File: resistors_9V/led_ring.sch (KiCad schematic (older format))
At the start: 15 parts, among them J1 Conn_01x02

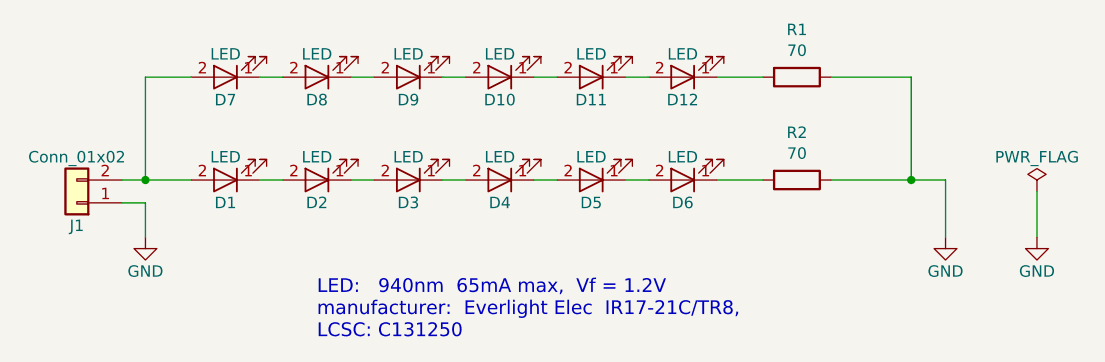
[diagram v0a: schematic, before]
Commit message: Finished 9V design w/ current limiting resistors.
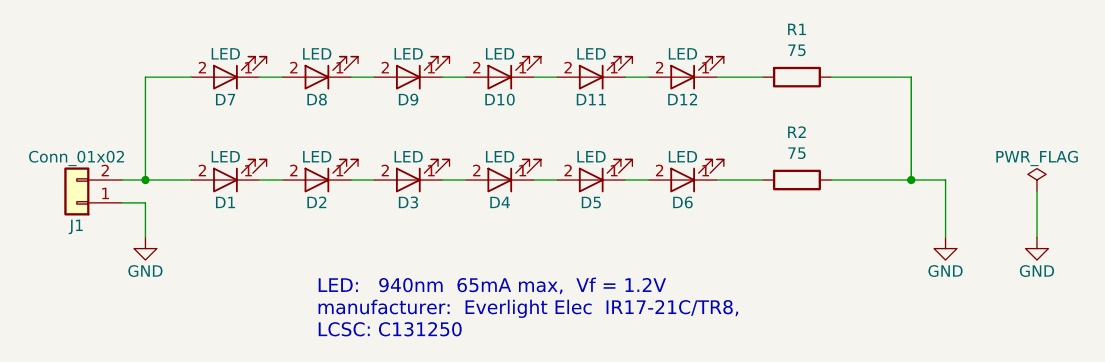
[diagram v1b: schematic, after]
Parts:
- D1, D10, D11, D12, D2, D3, D4, D5, D6, D7, D8, D9: footprint LEDs:LED_0805_HandSoldering -> LED_SMD:LED_0805_2012Metric
- R1, R2: value 70 -> 75; footprint (none) -> Resistor_SMD:R_0805_2012Metric
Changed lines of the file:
@@
 F 0 "D1" H 3650 1800 50  0000 C CNN
 F 1 "LED" H 3650 1600 50  0000 C CNN
-F 2 "LEDs:LED_0805_HandSoldering" H 3650 1700 50  0001 C CNN
+F 2 "LED_SMD:LED_0805_2012Metric" H 3650 1700 50  0001 C CNN
 F 3 "" H 3650 1700 50  0001 C CNN
 	1    3650 1700
@@
 F 0 "D2" H 4050 1800 50  0000 C CNN
 F 1 "LED" H 4050 1600 50  0000 C CNN
-F 2 "LEDs:LED_0805_HandSoldering" H 4050 1700 50  0001 C CNN
+F 2 "LED_SMD:LED_0805_2012Metric" H 4050 1700 50  0001 C CNN
 F 3 "" H 4050 1700 50  0001 C CNN
 	1    4050 1700
@@
 F 0 "D3" H 4450 1800 50  0000 C CNN
 F 1 "LED" H 4450 1600 50  0000 C CNN
-F 2 "LEDs:LED_0805_HandSoldering" H 4450 1700 50  0001 C CNN
+F 2 "LED_SMD:LED_0805_2012Metric" H 4450 1700 50  0001 C CNN
 F 3 "" H 4450 1700 50  0001 C CNN
 	1    4450 1700
@@
 F 0 "D4" H 4850 1800 50  0000 C CNN
 F 1 "LED" H 4850 1600 50  0000 C CNN
-F 2 "LEDs:LED_0805_HandSoldering" H 4850 1700 50  0001 C CNN
+F 2 "LED_SMD:LED_0805_2012Metric" H 4850 1700 50  0001 C CNN
 F 3 "" H 4850 1700 50  0001 C CNN
 	1    4850 1700
@@
 F 0 "D5" H 5250 1800 50  0000 C CNN
 F 1 "LED" H 5250 1600 50  0000 C CNN
-F 2 "LEDs:LED_0805_HandSoldering" H 5250 1700 50  0001 C CNN
+F 2 "LED_SMD:LED_0805_2012Metric" H 5250 1700 50  0001 C CNN
 F 3 "" H 5250 1700 50  0001 C CNN
 	1    5250 1700
@@
 F 0 "D6" H 5650 1800 50  0000 C CNN
 F 1 "LED" H 5650 1600 50  0000 C CNN
-F 2 "LEDs:LED_0805_HandSoldering" H 5650 1700 50  0001 C CNN
+F 2 "LED_SMD:LED_0805_2012Metric" H 5650 1700 50  0001 C CNN
 F 3 "" H 5650 1700 50  0001 C CNN
 	1    5650 1700
@@
 F 0 "D7" H 3650 1350 50  0000 C CNN
 F 1 "LED" H 3650 1150 50  0000 C CNN
-F 2 "LEDs:LED_0805_HandSoldering" H 3650 1250 50  0001 C CNN
+F 2 "LED_SMD:LED_0805_2012Metric" H 3650 1250 50  0001 C CNN
 F 3 "" H 3650 1250 50  0001 C CNN
 	1    3650 1250
@@
 F 0 "D8" H 4050 1350 50  0000 C CNN
 F 1 "LED" H 4050 1150 50  0000 C CNN
-F 2 "LEDs:LED_0805_HandSoldering" H 4050 1250 50  0001 C CNN
+F 2 "LED_SMD:LED_0805_2012Metric" H 4050 1250 50  0001 C CNN
 F 3 "" H 4050 1250 50  0001 C CNN
 	1    4050 1250
@@
 F 0 "D9" H 4450 1350 50  0000 C CNN
 F 1 "LED" H 4450 1150 50  0000 C CNN
-F 2 "LEDs:LED_0805_HandSoldering" H 4450 1250 50  0001 C CNN
+F 2 "LED_SMD:LED_0805_2012Metric" H 4450 1250 50  0001 C CNN
 F 3 "" H 4450 1250 50  0001 C CNN
 	1    4450 1250
@@
 F 0 "D10" H 4850 1350 50  0000 C CNN
 F 1 "LED" H 4850 1150 50  0000 C CNN
-F 2 "LEDs:LED_0805_HandSoldering" H 4850 1250 50  0001 C CNN
+F 2 "LED_SMD:LED_0805_2012Metric" H 4850 1250 50  0001 C CNN
 F 3 "" H 4850 1250 50  0001 C CNN
 	1    4850 1250
@@
 F 0 "D11" H 5250 1350 50  0000 C CNN
 F 1 "LED" H 5250 1150 50  0000 C CNN
-F 2 "LEDs:LED_0805_HandSoldering" H 5250 1250 50  0001 C CNN
+F 2 "LED_SMD:LED_0805_2012Metric" H 5250 1250 50  0001 C CNN
 F 3 "" H 5250 1250 50  0001 C CNN
 	1    5250 1250
@@
 F 0 "D12" H 5650 1350 50  0000 C CNN
 F 1 "LED" H 5650 1150 50  0000 C CNN
-F 2 "LEDs:LED_0805_HandSoldering" H 5650 1250 50  0001 C CNN
+F 2 "LED_SMD:LED_0805_2012Metric" H 5650 1250 50  0001 C CNN
 F 3 "" H 5650 1250 50  0001 C CNN
 	1    5650 1250
@@
 P 6150 1250
 F 0 "R1" V 5943 1250 50  0000 C CNN
-F 1 "70" V 6034 1250 50  0000 C CNN
-F 2 "" V 6080 1250 50  0001 C CNN
+F 1 "75" V 6034 1250 50  0000 C CNN
+F 2 "Resistor_SMD:R_0805_2012Metric" V 6080 1250 50  0001 C CNN
 F 3 "~" H 6150 1250 50  0001 C CNN
 	1    6150 1250
@@
 P 6150 1700
 F 0 "R2" V 5943 1700 50  0000 C CNN
-F 1 "70" V 6034 1700 50  0000 C CNN
-F 2 "" V 6080 1700 50  0001 C CNN
+F 1 "75" V 6034 1700 50  0000 C CNN
+F 2 "Resistor_SMD:R_0805_2012Metric" V 6080 1700 50  0001 C CNN
 F 3 "~" H 6150 1700 50  0001 C CNN
 	1    6150 1700
